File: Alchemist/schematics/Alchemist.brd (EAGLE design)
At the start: 55.9 x 58.8 mm, 89 parts, among them IC1 MC7805CDTG, IC6 OPA1679, J2 THONKICONN, J3 THONKICONN, Q901 BC846

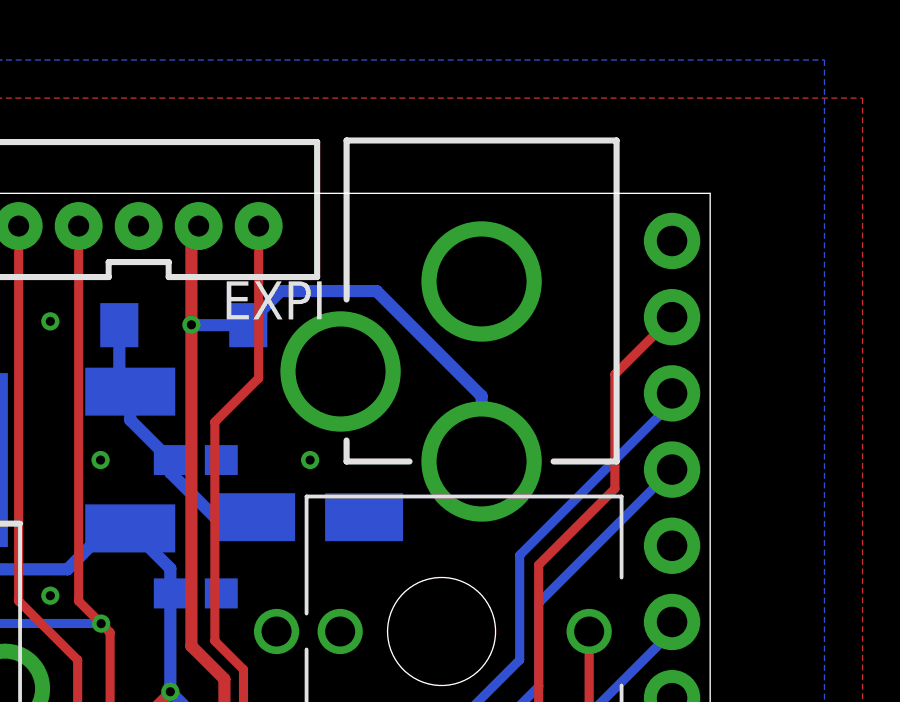
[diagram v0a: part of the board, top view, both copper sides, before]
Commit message: changed to slotted DC jacks
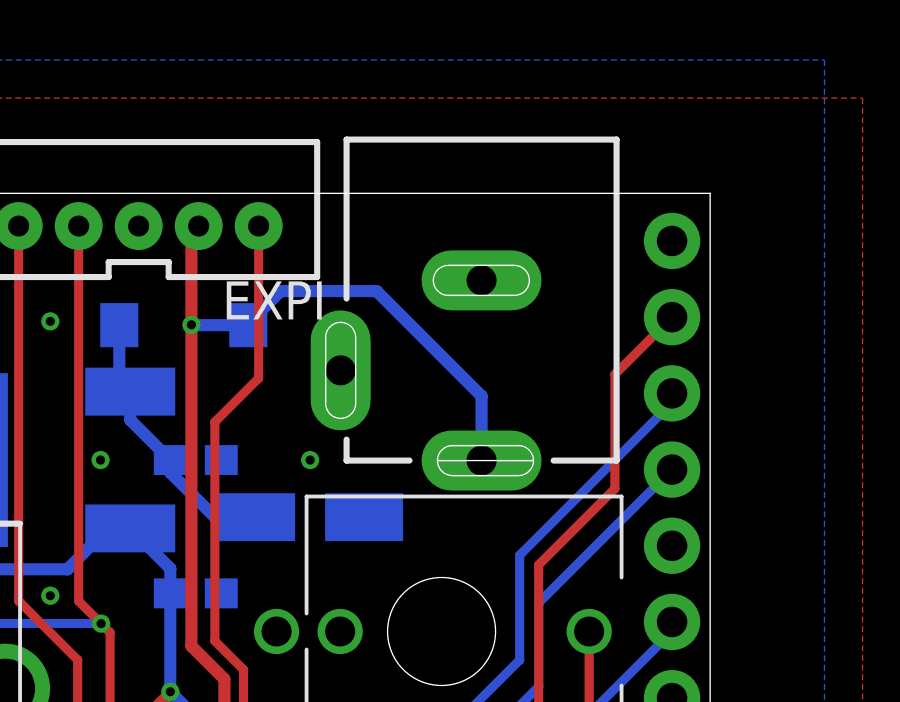
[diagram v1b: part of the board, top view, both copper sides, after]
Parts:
- J1: value (none) -> POWER_JACK; device SparkFun:POWER_JACK_PTH -> Rebel:DC_JACK_SLOT
- moved J1 2.92 mm to (50.8, 61.8)
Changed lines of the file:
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@@
 <attribute name="VALUE" x="40.621" y="57.2635" size="0.4064" layer="28" rot="MR0"/>
 </element>
-<element name="J1" library="SparkFun" package="POWER_JACK_PTH" value="" x="50.8" y="64.77" locked="yes" smashed="yes" rot="R180">
-<attribute name="VALUE" x="54.61" y="60.96" size="0.4064" layer="27" rot="R180"/>
+<element name="J1" library="Rebel" package="DC_JACK_SLOT" value="POWER_JACK" x="50.8" y="61.849" smashed="yes" rot="R180">
+<attribute name="VALUE" x="54.61" y="58.039" size="0.4064" layer="27" rot="R180"/>
 </element>
 <element name="J2" library="Rebel" package="THONKICONN" value="THONKICONN" x="49.4665" y="45.4025" locked="yes" rot="R270"/>
@@
 <wire x1="42.2275" y1="43.815" x2="42.2275" y2="12.7" width="0.4064" layer="1"/>
 <contactref element="J1" pad="PWR"/>
-<wire x1="50.8" y1="53.25" x2="50.8" y2="51.07" width="0.4064" layer="16"/>
+<wire x1="50.8" y1="53.25" x2="50.8" y2="51.1" width="0.4064" layer="16"/>
 <wire x1="50.8" y1="53.25" x2="47.3" y2="56.75" width="0.4064" layer="16"/>
 <wire x1="47.3" y1="56.75" x2="44.1" y2="56.75" width="0.4064" layer="16"/>

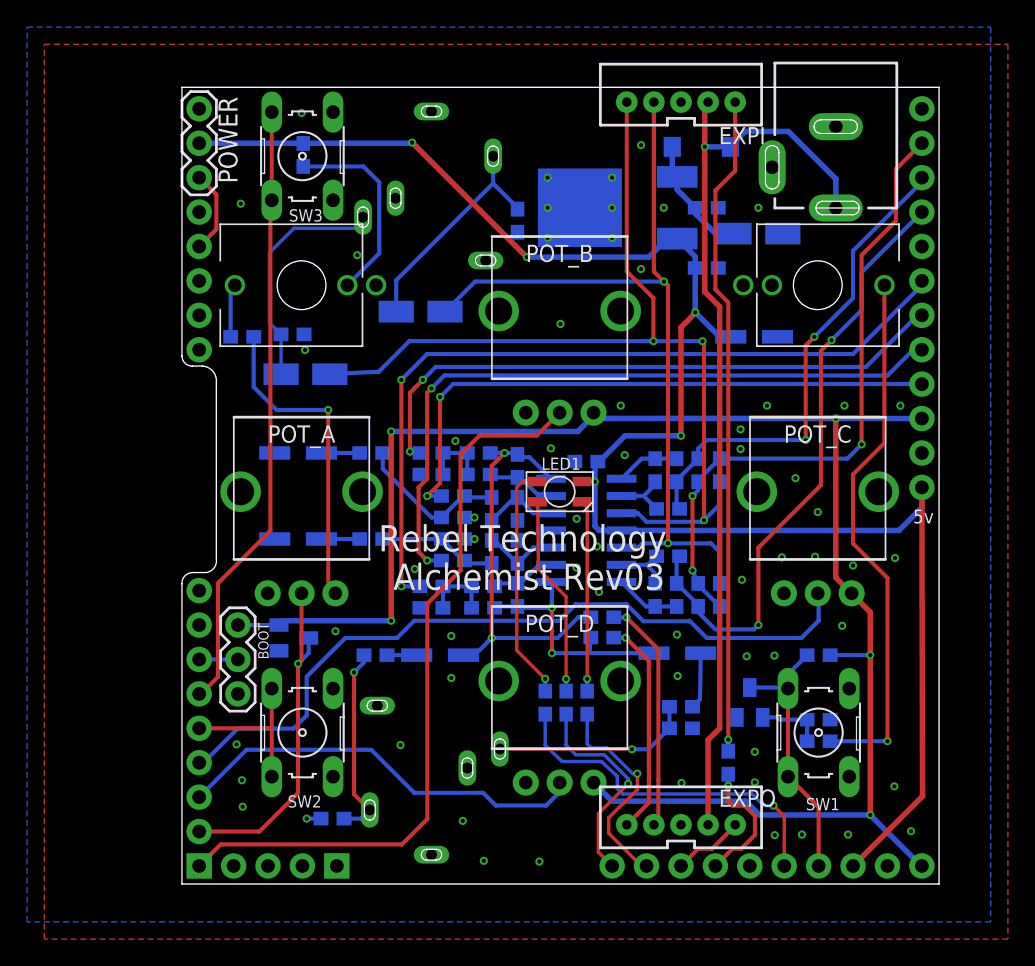
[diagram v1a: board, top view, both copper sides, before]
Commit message: renamed pots and switches
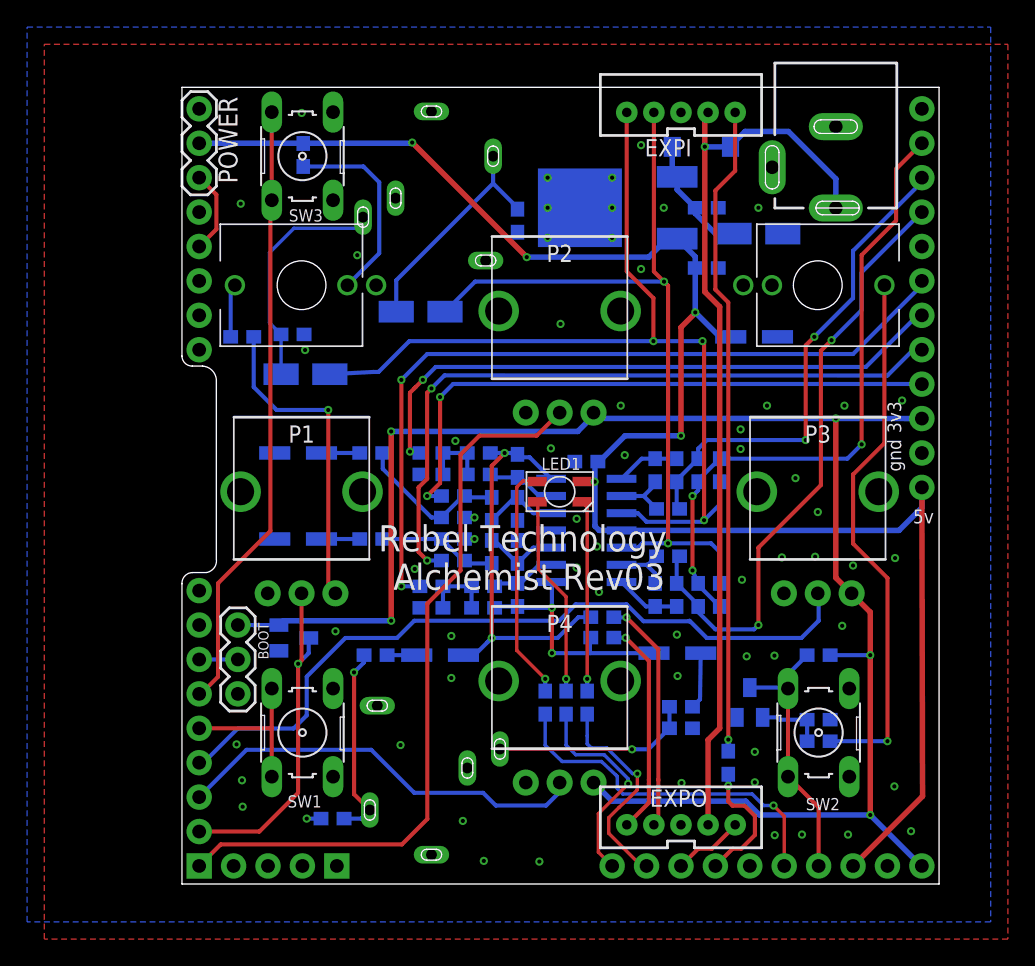
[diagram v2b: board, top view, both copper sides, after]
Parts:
- moved SW1 38.1 mm to (11.4, 12.4)
- moved SW2 38.1 mm to (49.5, 12.4)
- moved EXPI 0.76 mm to (39.4, 58.0)
- renumbered POT_A to P1, POT_B to P2, POT_C to P3, POT_D to P4
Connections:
- net GND: now also ANG2.6
- net GP7_TRIG: now also SW2.1, SW2.2; no longer SW1.1, SW1.2
- net GP8_TRIG: now also SW1.1, SW1.2; no longer SW2.1, SW2.2
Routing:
- net DC_IN_L: track 69.9 -> 69.1 mm
- net N$1: track 48.9 -> 48.1 mm
- net DC_IN_R: track 60.0 -> 59.3 mm
- net +9V: track 68.2 -> 67.5 mm

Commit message: removed alternative component values
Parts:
- C10, C7: value 4n7 / 6n8 C0G -> 4n7 C0G
- C18, C4: value 2n2 / 2n7 C0G -> 2n2 C0G
- C2, C23: value 1n / 1n5 C0G -> 1n C0G
- C20, C6, C9: value 220p / 470p C0G -> 220p C0G
- C3: value 220p / 470p -> 220p C0G
- R1, R18: value 2k / 2k32 -> 2k
- R10, R11: value 100R / 91R -> 100R
- R12, R404: value 5k1 / 4k99 -> 5k1
- R16, R35: value 5k1 / 4k42 -> 5k1
- R17, R39: value 1k / 1k33 -> 1k
- R19, R2: value 1k / 715R -> 1k
- R20, R7: value 1k / 1k5 -> 1k
- R3, R9: value 560R / 634R -> 560R

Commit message: changed op amp value to TS974
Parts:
- IC6: value OPA1679 -> TS974
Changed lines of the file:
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@@
 <?xml version="1.0" encoding="utf-8"?>
 <!DOCTYPE eagle SYSTEM "eagle.dtd">
-<eagle version="9.1.0">
+<eagle version="9.1.1">
 <drawing>
 <settings>
@@
 </element>
 <element name="P3" library="Rebel" package="POT-ALPS-RK09L1140" value="POT-ALPS-RK09L1140" x="49.4665" y="30.1625" locked="yes"/>
-<element name="IC6" library="linear" package="SO14" value="OPA1679" x="32.385" y="27.305" smashed="yes" rot="MR270">
+<element name="IC6" library="linear" package="SO14" value="TS974" x="32.385" y="27.305" smashed="yes" rot="MR270">
 <attribute name="NAME" x="33.02" y="27.1145" size="0.762" layer="26" rot="MR0"/>
 <attribute name="VALUE" x="34.29" y="21.463" size="1.27" layer="28" rot="MR0"/>

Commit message: reversed pieces so that all parts are seen from top / outside (frosted side up)
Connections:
- net ADC1 renamed A18_ADC1
- net ADC2 renamed A19_ADC2
- net ADC3 renamed A20_ADC3
- net ADC4 renamed A21_ADC4
- net GP10 renamed A14
- net GP11 renamed A13
- net GP1_LEDPWM renamed A1_LEDPWM2
- net GP2_LEDPWM renamed A2_LEDPWM3
- net GP3_USART_TX renamed A3_USART_TX
- net GP4_USART_RX renamed A4_USART_RX
- net GP5 renamed A5
- net GP6_LEDPWM renamed A6_LEDPWM1
- net GP7_TRIG renamed A7_SW2
- net GP8_TRIG renamed A17_SW1
- net GP9_TRIG renamed A16_SW3
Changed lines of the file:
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@@
 <wire x1="39.37" y1="42.291" x2="40.425" y2="43.346" width="0.4064" layer="1"/>
 </signal>
-<signal name="ADC1">
+<signal name="A18_ADC1">
 <contactref element="ADC" pad="4"/>
 <contactref element="P3" pad="2"/>
@@
 <wire x1="39.9675" y1="20.6" x2="40.005" y2="20.6375" width="0.3048" layer="16"/>
 </signal>
-<signal name="ADC4">
+<signal name="A21_ADC4">
 <contactref element="ADC" pad="1"/>
 <contactref element="P2" pad="2"/>
@@
 <wire x1="20.65" y1="21.9" x2="23.1" y2="24.35" width="0.3048" layer="1"/>
 </signal>
-<signal name="ADC2">
+<signal name="A19_ADC2">
 <contactref element="ADC" pad="3"/>
 <contactref element="P4" pad="2"/>
@@
 <wire x1="30.4165" y1="8.001" x2="30.4165" y2="8.6925" width="0.3048" layer="16"/>
 </signal>
-<signal name="ADC3">
+<signal name="A20_ADC3">
 <contactref element="ADC" pad="2"/>
 <contactref element="P1" pad="2"/>
@@
 <wire x1="37.465" y1="24.13" x2="36.83" y2="24.765" width="0.3048" layer="16"/>
 </signal>
-<signal name="GP10">
+<signal name="A14">
 <contactref element="TGP1-4" pad="2"/>
 </signal>
@@
 <wire x1="57.1375" y1="38.1125" x2="57.15" y2="38.1" width="0.3048" layer="16"/>
 </signal>
-<signal name="GP5">
+<signal name="A5">
 <contactref element="LGP1-5" pad="5"/>
 </signal>
-<signal name="GP4_USART_RX">
+<signal name="A4_USART_RX">
 <contactref element="LGP1-5" pad="4"/>
 <wire x1="41.91" y1="2.54" x2="41.945" y2="2.575" width="0.3048" layer="1"/>
@@
 <wire x1="43.815" y1="3.81" x2="44.831" y2="4.826" width="0.3048" layer="1"/>
 </signal>
-<signal name="GP9_TRIG">
+<signal name="A16_SW3">
 <contactref element="TGP1-4" pad="4"/>
 <contactref element="SW3" pad="2"/>
@@
 <wire x1="9.0694" y1="51.5763" x2="9.1694" y2="51.6763" width="0.3048" layer="1"/>
 </signal>
-<signal name="GP11">
+<signal name="A13">
 <contactref element="TGP1-4" pad="1"/>
 </signal>
@@
 <wire x1="23.28" y1="29.845" x2="21.6925" y2="28.2575" width="0.3048" layer="16"/>
 </signal>
-<signal name="GP1_LEDPWM">
+<signal name="A1_LEDPWM2">
 <contactref element="LGP1-5" pad="1"/>
 <contactref element="R21" pad="1"/>
@@
 <wire x1="33.274" y1="6.399" x2="35.475" y2="8.6" width="0.254" layer="1"/>
 </signal>
-<signal name="GP2_LEDPWM">
+<signal name="A2_LEDPWM3">
 <contactref element="LGP1-5" pad="2"/>
 <contactref element="R22" pad="1"/>
@@
 <wire x1="36.449" y1="2.54" x2="36.83" y2="2.54" width="0.254" layer="1"/>
 </signal>
-<signal name="GP6_LEDPWM">
+<signal name="A6_LEDPWM1">
 <contactref element="LGP6-7" pad="2"/>
 <contactref element="R28" pad="1"/>
@@
 <wire x1="30.6" y1="10.25" x2="33.5" y2="10.25" width="0.254" layer="16"/>
 </signal>
-<signal name="GP7_TRIG">
+<signal name="A7_SW2">
 <contactref element="LGP6-7" pad="1"/>
 <contactref element="SW2" pad="2"/>
@@
 <via x="41.12875" y="55.626" extent="1-16" drill="0.3048"/>
 </signal>
-<signal name="GP8_TRIG">
+<signal name="A17_SW1">
 <contactref element="SW1" pad="2"/>
 <contactref element="SW1" pad="1"/>
@@
 <wire x1="37" y1="7.2075" x2="35.37" y2="5.5775" width="0.3048" layer="1"/>
 </signal>
-<signal name="GP3_USART_TX">
+<signal name="A3_USART_TX">
 <contactref element="LGP1-5" pad="3"/>
 <contactref element="EXPO" pad="5"/>

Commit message: changed to op amp TS924
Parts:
- IC6: value TS974 -> TS924
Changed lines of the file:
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@@
 <?xml version="1.0" encoding="utf-8"?>
 <!DOCTYPE eagle SYSTEM "eagle.dtd">
-<eagle version="9.1.1">
+<eagle version="9.4.0">
 <drawing>
 <settings>
@@
 <attribute name="VALUE" x="20.955" y="20.51" size="1.27" layer="28" rot="MR180"/>
 </element>
-<element name="P3" library="Rebel" package="POT-ALPS-RK09L1140" value="POT-ALPS-RK09L1140" x="49.4665" y="30.1625" locked="yes"/>
-<element name="IC6" library="linear" package="SO14" value="TS974" x="32.385" y="27.305" smashed="yes" rot="MR270">
+<element name="P3" library="Rebel" package="POT-ALPS-RK09L1140" value="POT-ALPS-RK09L1140" x="49.4665" y="30.1625" locked="yes" smashed="yes">
+<attribute name="NAME" x="49.4665" y="33.7825" size="1.27" layer="25" font="vector" align="bottom-center"/>
+</element>
+<element name="IC6" library="linear" package="SO14" value="TS924" x="32.385" y="27.305" smashed="yes" rot="MR270">
 <attribute name="NAME" x="33.02" y="27.1145" size="0.762" layer="26" rot="MR0"/>
 <attribute name="VALUE" x="34.29" y="21.463" size="1.27" layer="28" rot="MR0"/>
@@
 <attribute name="NAME" x="41.430809375" y="13.0792625" size="0.762" layer="26" font="vector" rot="MR180" align="bottom-center"/>
 </element>
-<element name="P4" library="Rebel" package="POT-ALPS-RK09L1140" value="POT-ALPS-RK09L1140" x="30.4165" y="16.1925" locked="yes"/>
-<element name="P1" library="Rebel" package="POT-ALPS-RK09L1140" value="POT-ALPS-RK09L1140" x="11.3665" y="30.1625" locked="yes"/>
-<element name="P2" library="Rebel" package="POT-ALPS-RK09L1140" value="POT-ALPS-RK09L1140" x="30.4165" y="43.4975" locked="yes"/>
+<element name="P4" library="Rebel" package="POT-ALPS-RK09L1140" value="POT-ALPS-RK09L1140" x="30.4165" y="16.1925" locked="yes" smashed="yes">
+<attribute name="NAME" x="30.4165" y="19.8125" size="1.27" layer="25" font="vector" align="bottom-center"/>
+</element>
+<element name="P1" library="Rebel" package="POT-ALPS-RK09L1140" value="POT-ALPS-RK09L1140" x="11.3665" y="30.1625" locked="yes" smashed="yes">
+<attribute name="NAME" x="11.3665" y="33.7825" size="1.27" layer="25" font="vector" align="bottom-center"/>
+</element>
+<element name="P2" library="Rebel" package="POT-ALPS-RK09L1140" value="POT-ALPS-RK09L1140" x="30.4165" y="43.4975" locked="yes" smashed="yes">
+<attribute name="NAME" x="30.4165" y="47.1175" size="1.27" layer="25" font="vector" align="bottom-center"/>
+</element>
 <element name="JIN" library="con-lumberg" package="1503_09" value="1503_09" x="20.955" y="60.325" locked="yes" smashed="yes" rot="MR0">
 <attribute name="MF" value="" x="20.955" y="60.325" size="0.3048" layer="28" rot="MR0" display="off"/>
@@
 <attribute name="VALUE" x="54.61" y="58.039" size="0.4064" layer="27" rot="R180"/>
 </element>
-<element name="J2" library="Rebel" package="THONKICONN" value="THONKICONN" x="49.4665" y="45.4025" locked="yes" rot="R270"/>
-<element name="J3" library="Rebel" package="THONKICONN" value="THONKICONN" x="11.3665" y="45.4025" locked="yes" rot="R90"/>
+<element name="J2" library="Rebel" package="THONKICONN" value="THONKICONN" x="49.4665" y="45.4025" locked="yes" smashed="yes" rot="R270">
+<attribute name="NAME" x="52.0065" y="45.4025" size="1.27" layer="104" font="vector" rot="R270" align="bottom-center"/>
+</element>
+<element name="J3" library="Rebel" package="THONKICONN" value="THONKICONN" x="11.3665" y="45.4025" locked="yes" smashed="yes" rot="R90">
+<attribute name="NAME" x="8.8265" y="45.4025" size="1.27" layer="104" font="vector" rot="R90" align="bottom-center"/>
+</element>
 <element name="R21" library="Rebel" package="0603" value="1k" x="30.8925" y="14.5925" smashed="yes" rot="MR90">
 <attribute name="NAME" x="30.51359375" y="12.236446875" size="0.762" layer="26" font="vector" rot="MR90" align="bottom-center"/>
